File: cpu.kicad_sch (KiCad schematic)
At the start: 29 parts, among them J1 USB_C_Receptacle, SW1 TL3342F160QG/TR, SW2 TL3342F160QG/TR, U4 RP2040, U5 LM4040DBZ-3, U6 W25Q32JVSS, Y1 Crystal

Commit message: Small corrections
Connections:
- net XIN: no longer R9.2
- net XOUT: now also R9.2; no longer C13.1, R9.1, Y1.1
- new net: C13.1, R9.1, Y1.1
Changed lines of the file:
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@@
   (junction (at 218.44 38.1) (diameter 0) (color 0 0 0 0)
   )
+  (junction (at 33.02 162.56) (diameter 0) (color 0 0 0 0)
+  )
+  (junction (at 218.44 31.75) (diameter 0) (color 0 0 0 0)
+  )
+  (junction (at 104.775 139.7) (diameter 0) (color 0 0 0 0)
+  )
+  (junction (at 112.395 35.56) (diameter 0) (color 0 0 0 0)
+  )
+  (junction (at 83.82 162.56) (diameter 0) (color 0 0 0 0)
+  )
+  (junction (at 71.12 162.56) (diameter 0) (color 0 0 0 0)
+  )
+  (junction (at 234.95 19.05) (diameter 0) (color 0 0 0 0)
+  )
+  (junction (at 99.695 48.26) (diameter 0) (color 0 0 0 0)
+  )
+  (junction (at 45.72 162.56) (diameter 0) (color 0 0 0 0)
+  )
   (junction (at 247.015 98.425) (diameter 0) (color 0 0 0 0)
-  )
-  (junction (at 33.02 162.56) (diameter 0) (color 0 0 0 0)
-  )
-  (junction (at 218.44 31.75) (diameter 0) (color 0 0 0 0)
-  )
-  (junction (at 104.775 139.7) (diameter 0) (color 0 0 0 0)
-  )
-  (junction (at 112.395 35.56) (diameter 0) (color 0 0 0 0)
-  )
-  (junction (at 83.82 162.56) (diameter 0) (color 0 0 0 0)
-  )
-  (junction (at 71.12 162.56) (diameter 0) (color 0 0 0 0)
-  )
-  (junction (at 234.95 19.05) (diameter 0) (color 0 0 0 0)
-  )
-  (junction (at 99.695 48.26) (diameter 0) (color 0 0 0 0)
-  )
-  (junction (at 45.72 162.56) (diameter 0) (color 0 0 0 0)
   )
   (junction (at 109.855 45.72) (diameter 0) (color 0 0 0 0)
@@
     (stroke (width 0) (type default) (color 0 0 0 0))
   )
+  (wire (pts (xy 247.015 95.25) (xy 247.015 98.425))
+    (stroke (width 0) (type default) (color 0 0 0 0))
+  )
   (wire (pts (xy 73.025 111.76) (xy 79.375 111.76))
     (stroke (width 0) (type default) (color 0 0 0 0))
@@
     (stroke (width 0) (type default) (color 0 0 0 0))
   )
-  (wire (pts (xy 247.015 98.425) (xy 247.015 84.455))
-    (stroke (width 0) (type default) (color 0 0 0 0))
-  )
   (wire (pts (xy 141.605 66.04) (xy 130.175 66.04))
     (stroke (width 0) (type default) (color 0 0 0 0))
@@
     (stroke (width 0) (type default) (color 0 0 0 0))
   )
+  (wire (pts (xy 247.015 84.455) (xy 247.015 87.63))
+    (stroke (width 0) (type default) (color 0 0 0 0))
+  )
   (wire (pts (xy 46.99 19.05) (xy 46.99 21.59))
     (stroke (width 0) (type default) (color 0 0 0 0))
   )
-  (wire (pts (xy 234.315 84.455) (xy 227.965 84.455))
-    (stroke (width 0) (type default) (color 0 0 0 0))
-  )
   (wire (pts (xy 141.605 73.66) (xy 130.175 73.66))
     (stroke (width 0) (type default) (color 0 0 0 0))
@@
     (stroke (width 0) (type default) (color 0 0 0 0))
   )
-  (wire (pts (xy 247.015 84.455) (xy 241.935 84.455))
-    (stroke (width 0) (type default) (color 0 0 0 0))
-  )
   (wire (pts (xy 109.855 45.72) (xy 114.935 45.72))
     (stroke (width 0) (type default) (color 0 0 0 0))
@@
     (effects (font (size 1.27 1.27)) (justify right bottom))
   )
-  (label "XOUT" (at 241.935 84.455 0)
+  (label "XOUT" (at 247.015 84.455 0)
     (effects (font (size 1.27 1.27)) (justify left bottom))
   )
@@
     (effects (font (size 1.27 1.27)) (justify left bottom))
   )
-  (hierarchical_label "GPIO23" (shape output) (at 141.605 114.3 0)
+  (hierarchical_label "GPIO10" (shape output) (at 141.605 81.28 0)
     (effects (font (size 1.27 1.27)) (justify left))
   )
@@
     (pin "1")
   )
-  (symbol (lib_id "Device:R") (at 238.125 84.455 270) (unit 1)
-    (in_bom yes) (on_board yes)
-    (property "Reference" "R9" (id 0) (at 238.125 86.995 90))
-    (property "Value" "1k" (id 1) (at 238.125 84.455 90))
-    (property "Footprint" "Resistor_SMD:R_0603_1608Metric" (id 2) (at 238.125 82.677 90)
-      (effects (font (size 1.27 1.27)) hide)
-    )
-    (property "Datasheet" "~" (id 3) (at 238.125 84.455 0)
-      (effects (font (size 1.27 1.27)) hide)
-    )
-    (pin "1")
-    (pin "2")
-  )
   (symbol (lib_id "TL3342F160QG_TR:TL3342F160QG{slash}TR") (at 170.18 65.405 0) (unit 1)
     (in_bom yes) (on_board yes) (fields_autoplaced)
@@
     (pin "4")
   )
+  (symbol (lib_id "Device:R") (at 247.015 91.44 0) (mirror x) (unit 1)
+    (in_bom yes) (on_board yes)
+    (property "Reference" "R9" (id 0) (at 249.555 91.44 90))
+    (property "Value" "1k" (id 1) (at 247.015 91.44 90))
+    (property "Footprint" "Resistor_SMD:R_0603_1608Metric" (id 2) (at 245.237 91.44 90)
+      (effects (font (size 1.27 1.27)) hide)
+    )
+    (property "Datasheet" "~" (id 3) (at 247.015 91.44 0)
+      (effects (font (size 1.27 1.27)) hide)
+    )
+    (pin "1")
+    (pin "2")
+  )
   (symbol (lib_id "Device:R") (at 79.375 43.815 0) (unit 1)

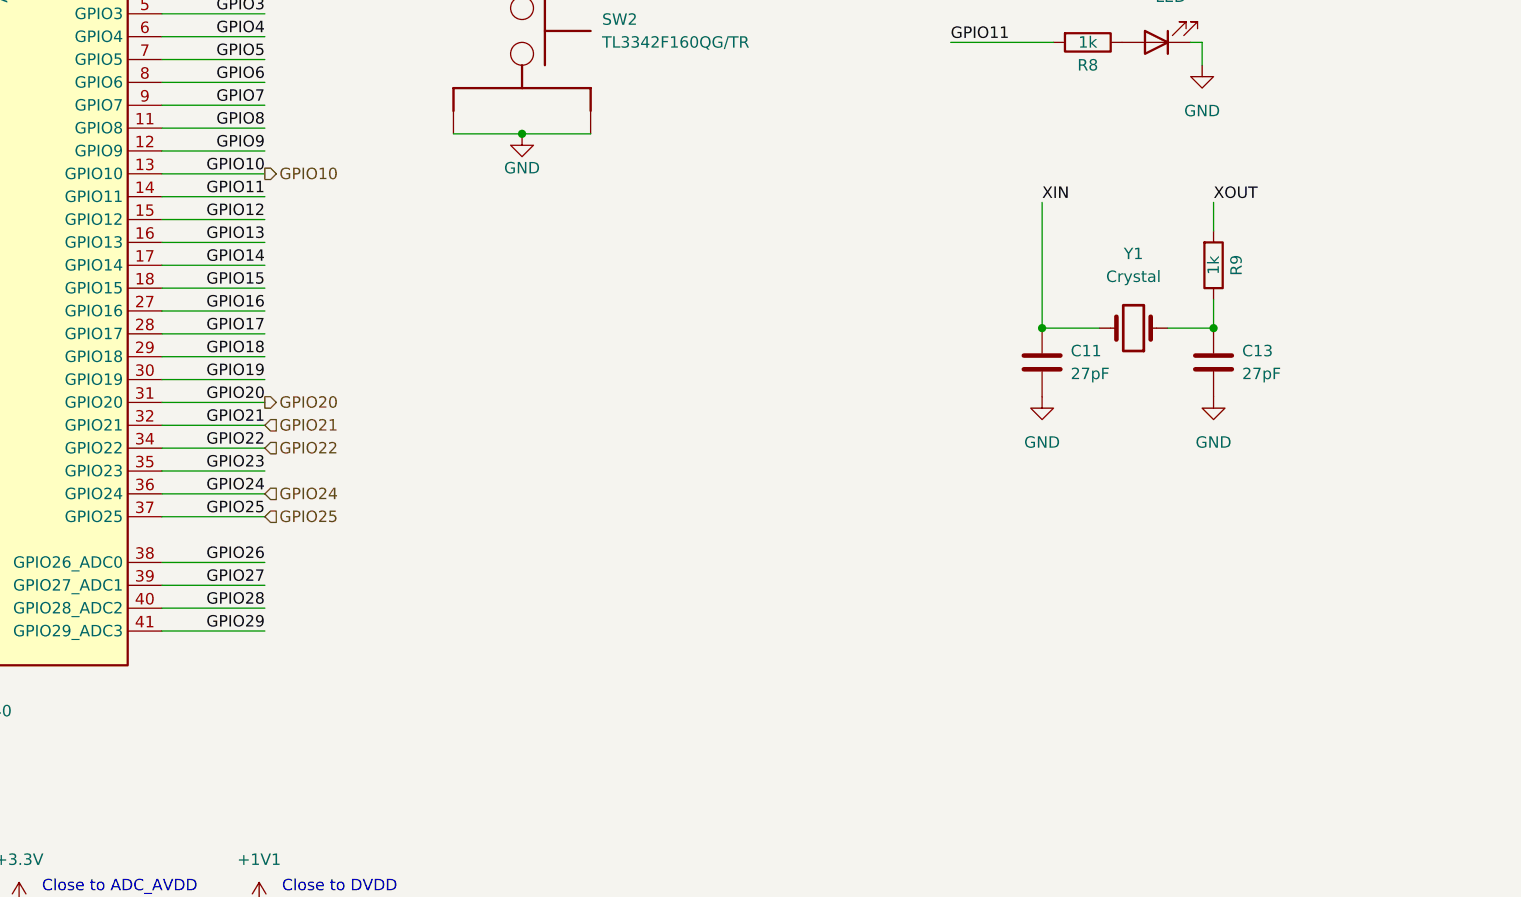
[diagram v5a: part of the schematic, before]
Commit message: Added CAN transsiver to RP2040
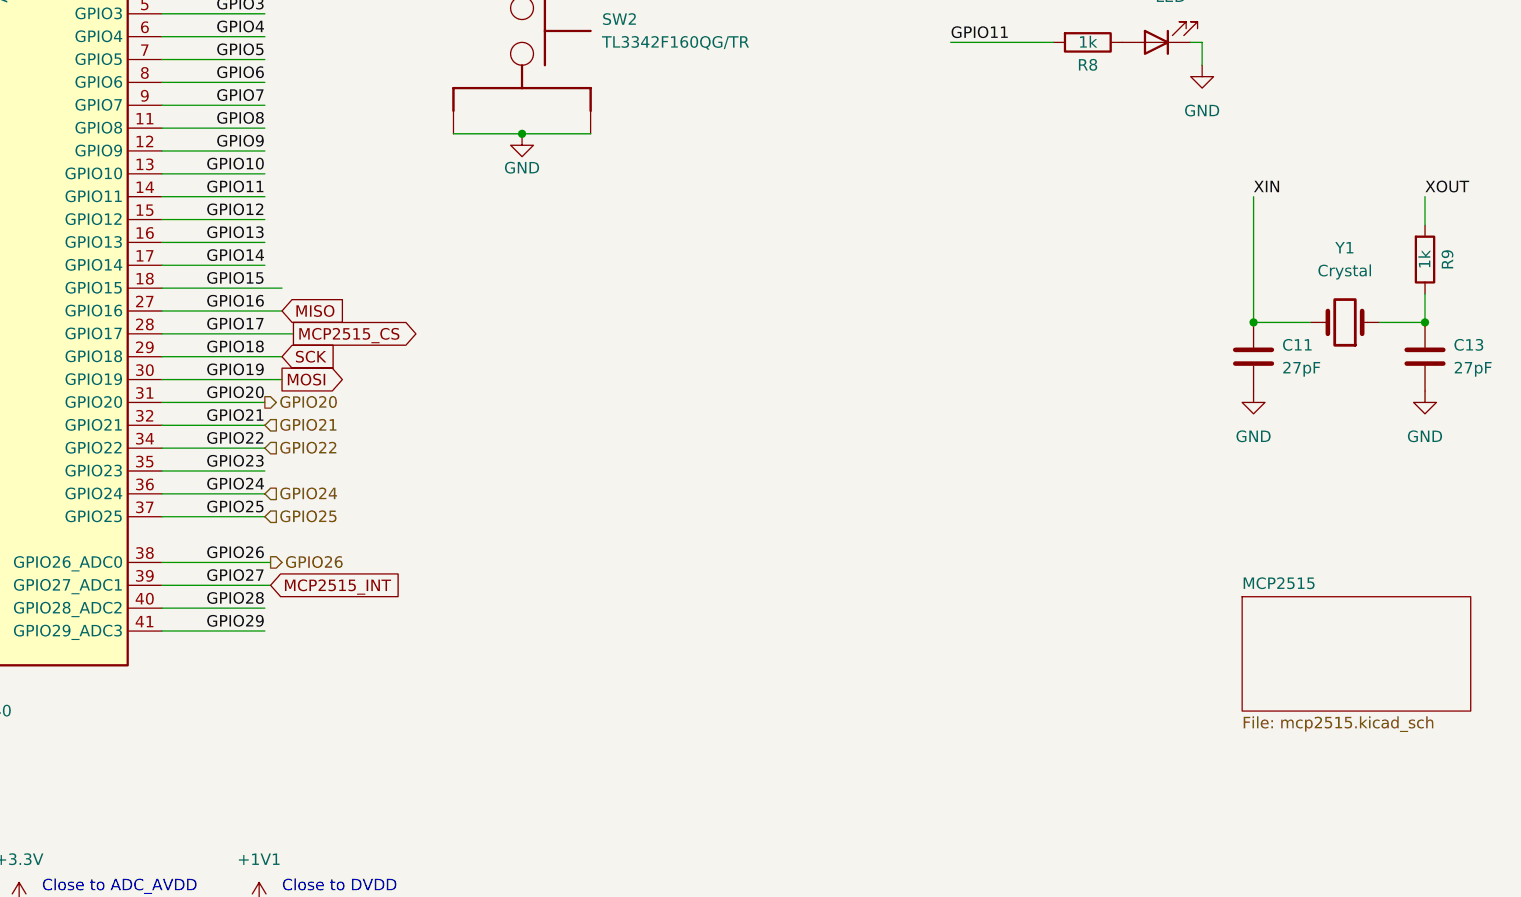
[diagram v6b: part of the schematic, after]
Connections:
- net GPIO16 renamed MISO
- net GPIO17 renamed MCP2515_CS
- net GPIO18 renamed SCK
- net GPIO19 renamed MOSI
- net GPIO27 renamed MCP2515_INT
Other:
- added sheet MCP2515 (mcp2515.kicad_sch)
- moved on the sheet: C11, C13, R9, Y1

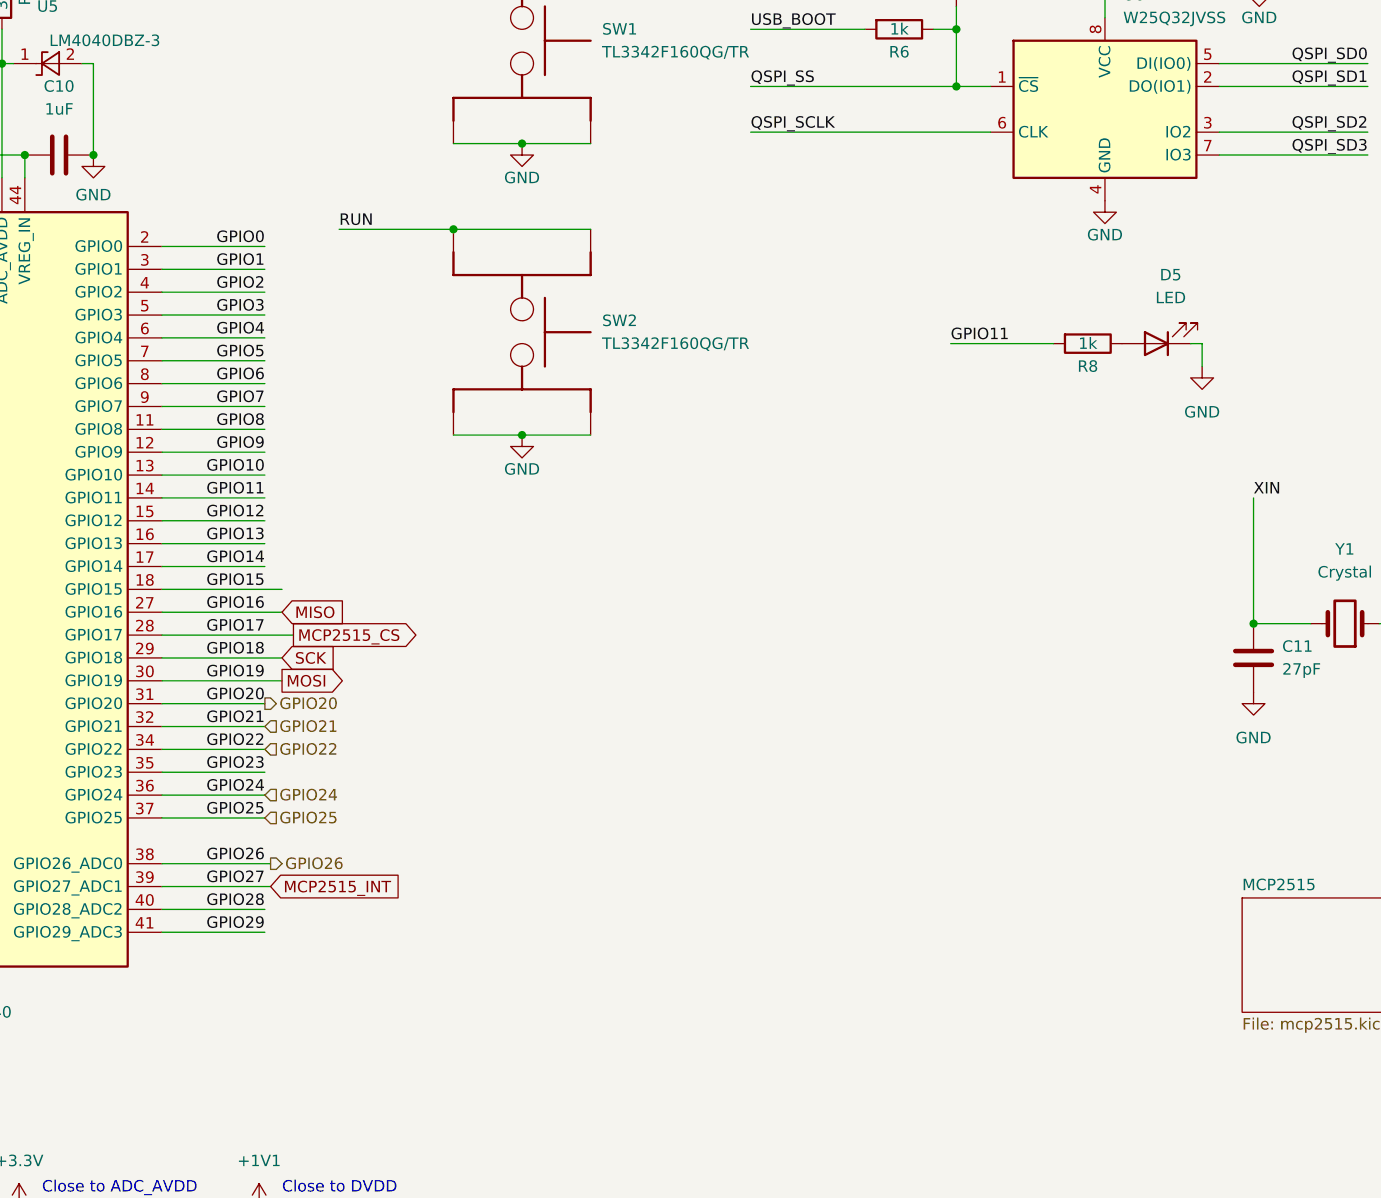
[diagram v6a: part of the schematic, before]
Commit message: Added DS1307 RTC and micro SD card
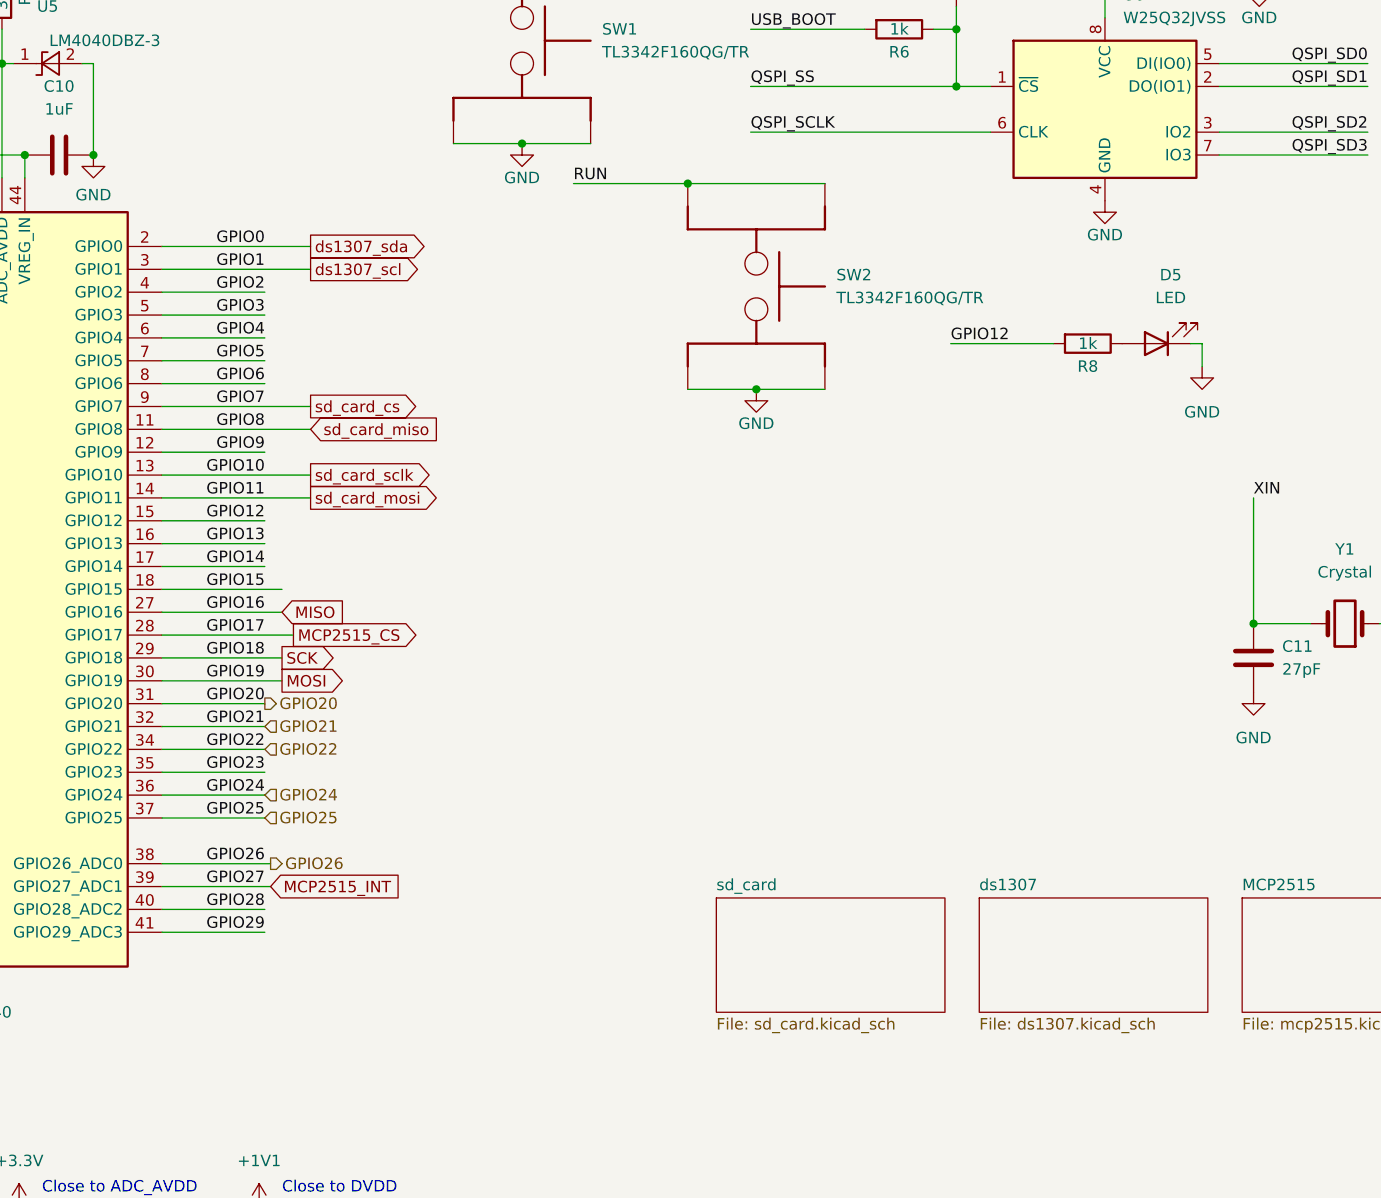
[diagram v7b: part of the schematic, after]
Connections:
- net GPIO12: now also R8.2
- net GPIO0 renamed ds1307_sda
- net GPIO1 renamed ds1307_scl
- net GPIO10 renamed sd_card_sclk
- net GPIO11 renamed sd_card_mosi
- net sd_card_mosi: no longer R8.2
- net GPIO7 renamed sd_card_cs
- net GPIO8 renamed sd_card_miso
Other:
- added sheet ds1307 (ds1307.kicad_sch)
- added sheet sd_card (sd_card.kicad_sch)
- moved on the sheet: SW2
